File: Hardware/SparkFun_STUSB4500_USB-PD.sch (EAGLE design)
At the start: 47 parts, among them J4 QWIIC, Q1 7.6A/30V/29mΩ, U1 STUSB4500, U2 3.3V

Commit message: v01
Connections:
- net ALERT renamed !ALERT
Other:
- note added: "ADDR0 and ADDR1 sets I2C address: ADDR0 | ADDR1 | Address 0 | 0 | 0x28* 1 | 0 | 0x29 0 | 1 | 0x2A 1 | 1 | 0x2B * Default Address"
- note added: "VIN: 4.1 - 22V"
- note removed: "ADDR0 and ADDR1 sets I2C address: ADDR0 | ADDR1 | Address 0 | 0 | 0x28 1 | 0 | 0x29 0 | 1 | 0x2A 1 | 1 | 0x2B"
- note removed: "VCC: 4.1 - 22V"

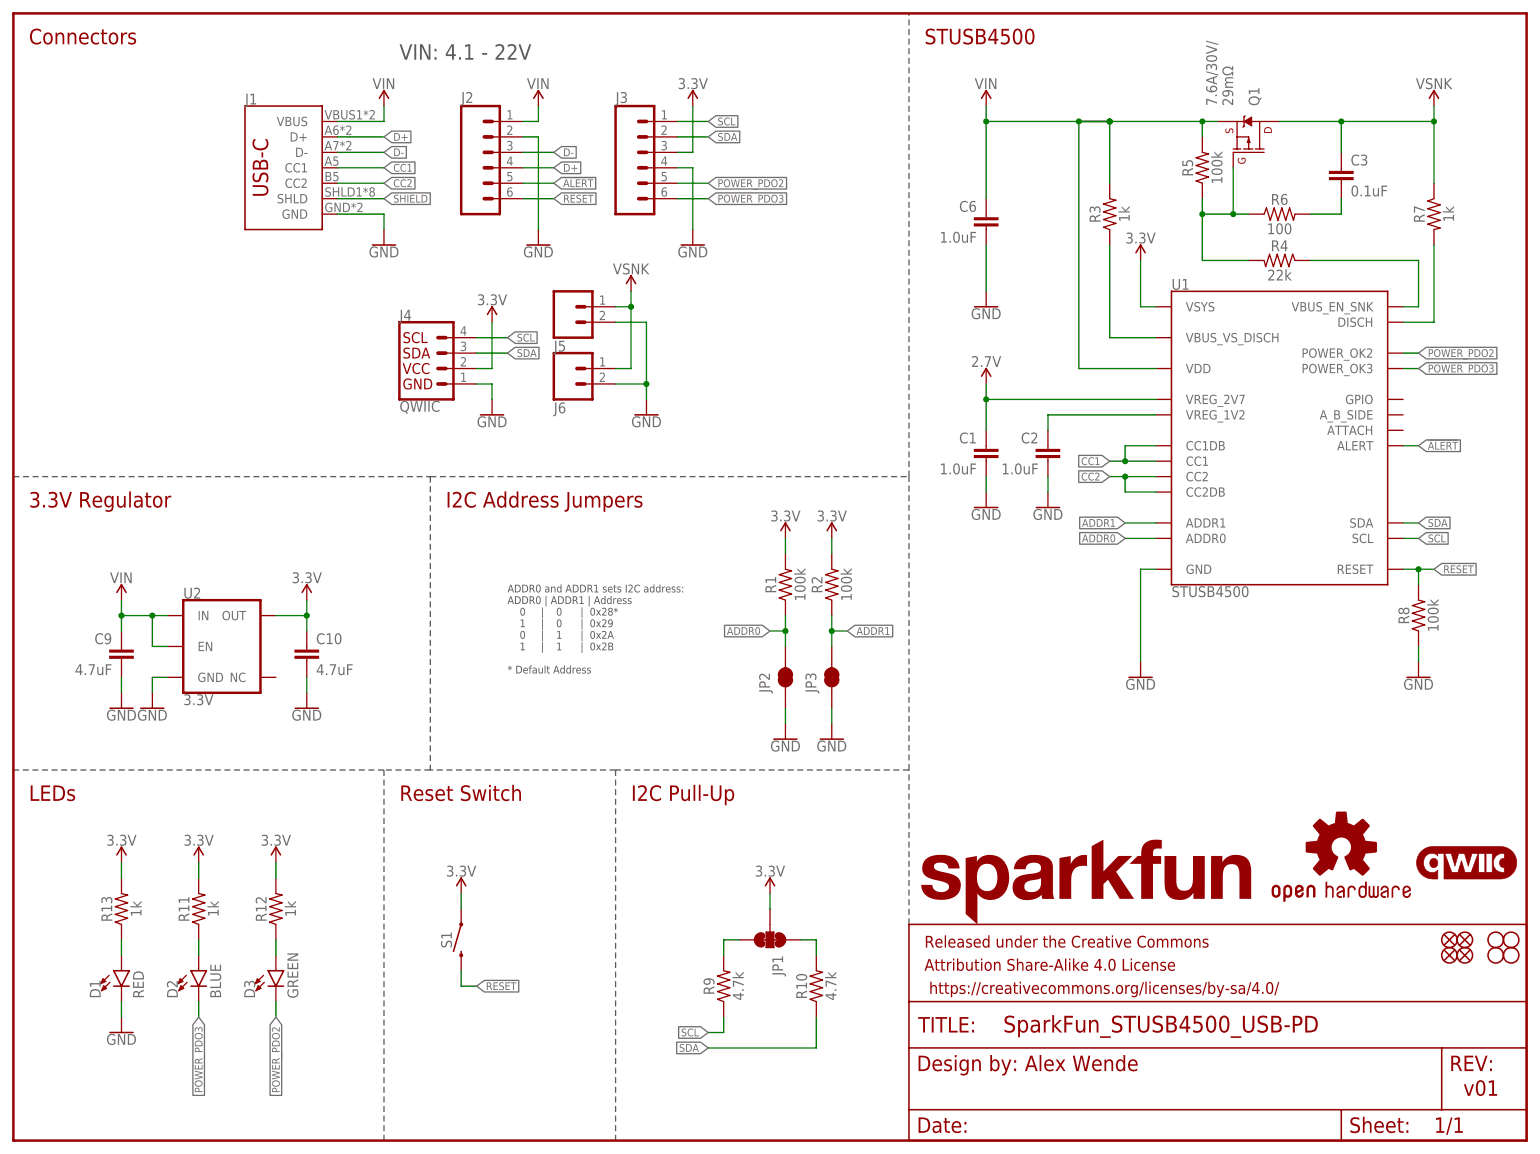
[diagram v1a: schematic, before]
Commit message: v02
-Added ESD protection diodes to VIN,VSNK, CC1, CC2
-Removed 3.3V LDO and replaced with the internal 2.7V regulated output of the STUSB4500.
-Added reverse current protection to the 2.7V regulator when VDD > 2.7V
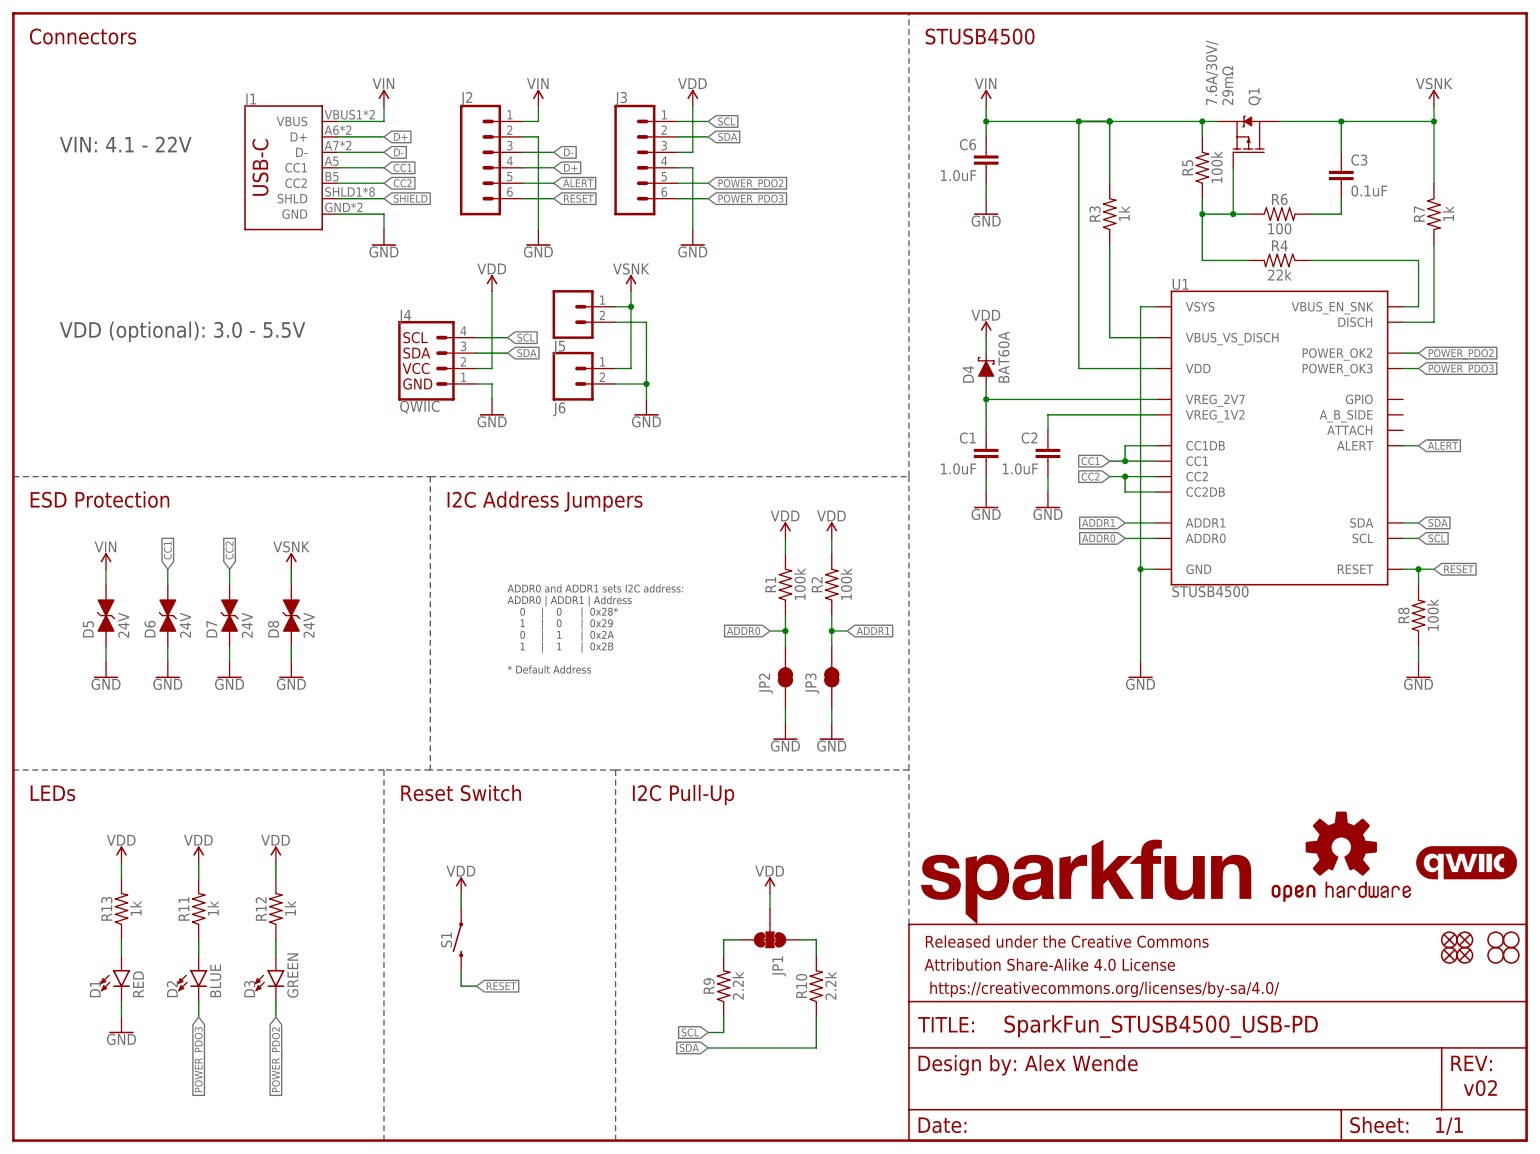
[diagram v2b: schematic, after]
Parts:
- removed C10, C9: 4.7uF, SparkFun-Capacitors:4.7UF-0603-35V-(20%)
- removed U2: 3.3V, SparkFun-IC-Power:AP7380-33W5-7
- added D4: BAT60A, SparkFun-DiscreteSemi:DIODE-SCHOTTKY-BAT60A
- added D5, D6, D7, D8: 24V, SparkFun-DiscreteSemi:DIODE_TVS
- LOGO3: value QWIIC_LOGO_5MM -> QWIIC_LOGO_3MM; device SparkFun-Aesthetics:QWIIC_LOGO_5MM -> SparkFun-Aesthetics:QWIIC_LOGO_3MM
- Q1: value 7.6A/30V/29mΩ -> 9A/30V/15mΩ; device SparkFun-DiscreteSemi:MOSFET_PCH-SI2369DS-T1-GE3 -> stusb4500:MOSFET_PCH-STL9P3LLH6
- R10, R9: value 4.7k -> 2.2k; device SparkFun-Resistors:4.7KOHM-0603-1/10W-1% -> SparkFun-Resistors:2.2KOHM-0603-1/10W-1%
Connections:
- removed net 3.3V: C10.1, J3.3, J4.2, JP1.2, R1.2, R11.2, R12.2, R13.2, R2.2, S1.1, U1.VSYS, U2.OUT
- new net VDD: D4.C, J3.3, J4.2, JP1.2, R1.2, R11.2, R12.2, R13.2, R2.2, S1.1
- net 2.7V: now also D4.A
- net CC1: now also D6.C
- net CC2: now also D7.C
- net GND: now also D5.A, D6.A, D7.A, D8.A, U1.VSYS; no longer C10.2, C9.2, U2.GND
- net VIN: now also D5.C; no longer C9.1, U2.EN, U2.IN
- net VSNK: now also D8.C
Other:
- note added: "ESD Protection"
- note added: "VDD (optional): 3.0 - 5.5V"
- note added: "v02"
- note removed: "3.3V Regulator"
- note removed: "v01"
- moved on the sheet: C6

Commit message: v20
- Updated Labels
- Connected VSYS to VDD
- Replaced Power LED with GPIO LED
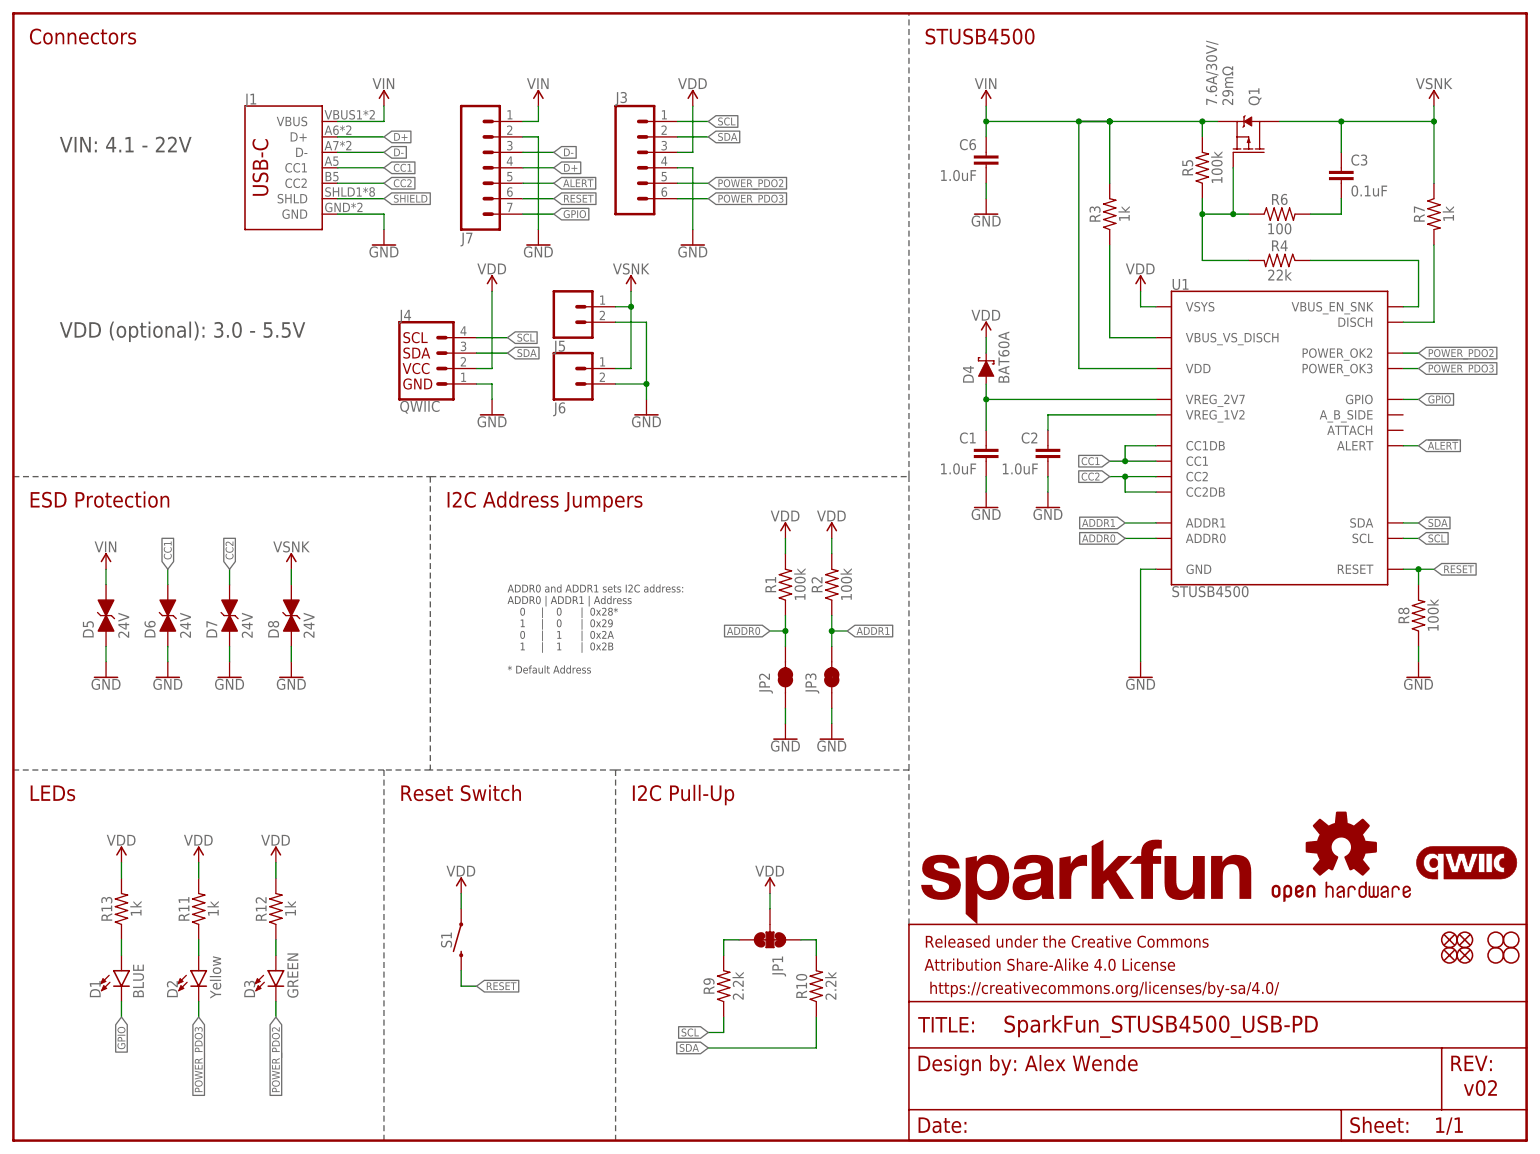
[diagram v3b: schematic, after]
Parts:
- removed J2: (no value), SparkFun-Connectors:CONN_06NO_SILK_NO_POP
- added J7: (no value), SparkFun-Connectors:CONN_07NO_SILK
- D1: value RED -> BLUE; device SparkFun-LED:LED-RED0603 -> SparkFun-LED:LED-BLUE0603
- D2: value BLUE -> Yellow; device SparkFun-LED:LED-BLUE0603 -> SparkFun-LED:LED-YELLOW0603
- LOGO3: value QWIIC_LOGO_3MM -> QWIIC_LOGO_5MM; device SparkFun-Aesthetics:QWIIC_LOGO_3MM -> SparkFun-Aesthetics:QWIIC_LOGO_5MM
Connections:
- new net GPIO: D1.C, J7.7, U1.GPIO
- net !ALERT: now also J7.5; no longer J2.5
- net D+: now also J7.4; no longer J2.4
- net D-: now also J7.3; no longer J2.3
- net GND: now also J7.2; no longer D1.C, J2.2, U1.VSYS
- net RESET: now also J7.6; no longer J2.6
- net VDD: now also U1.VSYS
- net VIN: now also J7.1; no longer J2.1
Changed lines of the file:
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@@
 <part name="SUPPLY10" library="SparkFun-PowerSymbols" deviceset="VOUT" device="" value="VSNK"/>
 <part name="S1" library="SparkFun-Switches" deviceset="MOMENTARY-SWITCH-SPST" device="-SMD-4.6X2.8MM" value=""/>
-<part name="D1" library="SparkFun-LED" deviceset="LED-RED" device="0603" value="RED"/>
+<part name="D1" library="SparkFun-LED" deviceset="LED-BLUE" device="0603" value="BLUE"/>
 <part name="R13" library="SparkFun-Resistors" deviceset="1KOHM" device="-0603-1/10W-1%" value="1k"/>
-<part name="GND16" library="SparkFun-PowerSymbols" deviceset="GND" device=""/>
-<part name="J2" library="SparkFun-Connectors" deviceset="CONN_06" device="NO_SILK_NO_POP"/>
 <part name="J3" library="SparkFun-Connectors" deviceset="CONN_06" device="NO_SILK_NO_POP"/>
-<part name="D2" library="SparkFun-LED" deviceset="LED-BLUE" device="0603" value="BLUE"/>
+<part name="D2" library="SparkFun-LED" deviceset="LED-YELLOW" device="0603" value="Yellow"/>
 <part name="D3" library="SparkFun-LED" deviceset="LED-GREEN" device="0603" value="GREEN"/>
 <part name="R11" library="SparkFun-Resistors" deviceset="1KOHM" device="-0603-1/10W-1%" value="1k"/>
@@
 <part name="LOGO1" library="SparkFun-Aesthetics" deviceset="OSHW-LOGO" device="S"/>
 <part name="LOGO2" library="SparkFun-Aesthetics" deviceset="SFE_LOGO_NAME" device=".1_INCH"/>
-<part name="LOGO3" library="SparkFun-Aesthetics" deviceset="QWIIC_LOGO" device="_3MM" value="QWIIC_LOGO_3MM"/>
+<part name="LOGO3" library="SparkFun-Aesthetics" deviceset="QWIIC_LOGO" device="_5MM" value="QWIIC_LOGO_5MM"/>
 <part name="GND10" library="SparkFun-PowerSymbols" deviceset="GND" device=""/>
 <part name="GND12" library="SparkFun-PowerSymbols" deviceset="GND" device=""/>
@@
 <part name="SUPPLY16" library="SparkFun-PowerSymbols" deviceset="VDD" device=""/>
 <part name="SUPPLY19" library="SparkFun-PowerSymbols" deviceset="VDD" device=""/>
+<part name="SUPPLY1" library="SparkFun-PowerSymbols" deviceset="VDD" device=""/>
+<part name="J7" library="SparkFun-Connectors" deviceset="CONN_07" device="NO_SILK"/>
 </parts>
 <sheets>
@@
 <attribute name="VALUE" x="19.304" y="38.1" size="1.778" layer="96" font="vector" rot="R90" align="top-center"/>
 </instance>
-<instance part="GND16" gate="1" x="17.78" y="17.78" smashed="yes">
-<attribute name="VALUE" x="17.78" y="17.526" size="1.778" layer="96" font="vector" align="top-center"/>
-</instance>
-<instance part="J2" gate="G$1" x="78.74" y="162.56" smashed="yes" rot="MR180">
-<attribute name="VALUE" x="73.66" y="172.466" size="1.778" layer="96" font="vector" rot="MR180"/>
-<attribute name="NAME" x="73.66" y="170.688" size="1.778" layer="95" font="vector"/>
-</instance>
 <instance part="J3" gate="G$1" x="104.14" y="162.56" smashed="yes" rot="MR180">
 <attribute name="VALUE" x="99.06" y="172.466" size="1.778" layer="96" font="vector" rot="MR180"/>
@@
 <attribute name="VALUE" x="134.62" y="101.854" size="1.778" layer="96" align="bottom-center"/>
 </instance>
+<instance part="SUPPLY1" gate="VDD" x="185.42" y="139.7" smashed="yes">
+<attribute name="VALUE" x="185.42" y="142.494" size="1.778" layer="96" align="bottom-center"/>
+</instance>
+<instance part="J7" gate="J1" x="78.74" y="162.56" smashed="yes" rot="MR180">
+<attribute name="VALUE" x="73.66" y="172.466" size="1.778" layer="96" font="vector" rot="MR180"/>
+<attribute name="NAME" x="73.66" y="149.352" size="1.778" layer="95" font="vector" rot="MR180"/>
+</instance>
 </instances>
 <busses>
@@
 </segment>
 <segment>
-<pinref part="D1" gate="G$1" pin="C"/>
-<pinref part="GND16" gate="1" pin="GND"/>
-<wire x1="17.78" y1="22.86" x2="17.78" y2="20.32" width="0.1524" layer="91"/>
-</segment>
-<segment>
 <pinref part="U1" gate="G$1" pin="GND"/>
 <pinref part="GND2" gate="1" pin="GND"/>
 <wire x1="187.96" y1="93.98" x2="185.42" y2="93.98" width="0.1524" layer="91"/>
 <wire x1="185.42" y1="93.98" x2="185.42" y2="78.74" width="0.1524" layer="91"/>
-<pinref part="U1" gate="G$1" pin="VSYS"/>
-<wire x1="187.96" y1="137.16" x2="185.42" y2="137.16" width="0.1524" layer="91"/>
-<wire x1="185.42" y1="137.16" x2="185.42" y2="93.98" width="0.1524" layer="91"/>
-<junction x="185.42" y="93.98"/>
-</segment>
-<segment>
-<pinref part="J2" gate="G$1" pin="2"/>
+</segment>
+<segment>
 <wire x1="83.82" y1="165.1" x2="86.36" y2="165.1" width="0.1524" layer="91"/>
 <pinref part="GND10" gate="1" pin="GND"/>
 <wire x1="86.36" y1="165.1" x2="86.36" y2="149.86" width="0.1524" layer="91"/>
+<pinref part="J7" gate="J1" pin="2"/>
 </segment>
 <segment>
@@
 </segment>
 <segment>
-<pinref part="J2" gate="G$1" pin="4"/>
 <wire x1="83.82" y1="160.02" x2="88.9" y2="160.02" width="0.1524" layer="91"/>
 <label x="88.9" y="160.02" size="1.27" layer="95" font="vector" rot="MR180" xref="yes"/>
+<pinref part="J7" gate="J1" pin="4"/>
 </segment>
 </net>
@@
 </segment>
 <segment>
-<pinref part="J2" gate="G$1" pin="3"/>
 <wire x1="83.82" y1="162.56" x2="88.9" y2="162.56" width="0.1524" layer="91"/>
 <label x="88.9" y="162.56" size="1.27" layer="95" font="vector" rot="MR180" xref="yes"/>
+<pinref part="J7" gate="J1" pin="3"/>
 </segment>
 </net>
@@
 </segment>
 <segment>
-<pinref part="J2" gate="G$1" pin="5"/>
 <wire x1="83.82" y1="157.48" x2="88.9" y2="157.48" width="0.1524" layer="91"/>
 <label x="88.9" y="157.48" size="1.27" layer="95" font="vector" rot="MR180" xref="yes"/>
+<pinref part="J7" gate="J1" pin="5"/>
 </segment>
 </net>
@@
 </segment>
 <segment>
-<pinref part="J2" gate="G$1" pin="6"/>
 <wire x1="83.82" y1="154.94" x2="88.9" y2="154.94" width="0.1524" layer="91"/>
 <label x="88.9" y="154.94" size="1.27" layer="95" font="vector" rot="MR180" xref="yes"/>
+<pinref part="J7" gate="J1" pin="6"/>
 </segment>
 </net>
@@
 </segment>
 <segment>
-<pinref part="J2" gate="G$1" pin="1"/>
 <wire x1="83.82" y1="167.64" x2="86.36" y2="167.64" width="0.1524" layer="91"/>
 <wire x1="86.36" y1="170.18" x2="86.36" y2="167.64" width="0.1524" layer="91"/>
 <pinref part="SUPPLY18" gate="G$1" pin="VIN"/>
+<pinref part="J7" gate="J1" pin="1"/>
 </segment>
 <segment>
@@
 <pinref part="SUPPLY5" gate="VDD" pin="VDD"/>
 </segment>
-</net>
+<segment>
+<pinref part="U1" gate="G$1" pin="VSYS"/>
+<wire x1="187.96" y1="137.16" x2="185.42" y2="137.16" width="0.1524" layer="91"/>
+<wire x1="185.42" y1="137.16" x2="185.42" y2="139.7" width="0.1524" layer="91"/>
+<pinref part="SUPPLY1" gate="VDD" pin="VDD"/>
+</segment>
+</net>
+<net name="GPIO" class="0">
+<segment>
+<pinref part="U1" gate="G$1" pin="GPIO"/>
+<wire x1="228.6" y1="121.92" x2="231.14" y2="121.92" width="0.1524" layer="91"/>
+<label x="231.14" y="121.92" size="1.27" layer="95" xref="yes"/>
+</segment>
+<segment>
+<pinref part="D1" gate="G$1" pin="C"/>
+<wire x1="17.78" y1="22.86" x2="17.78" y2="20.32" width="0.1524" layer="91"/>
+<label x="17.78" y="20.32" size="1.27" layer="95" rot="R270" xref="yes"/>
+</segment>
+<segment>
+<pinref part="J7" gate="J1" pin="7"/>
+<wire x1="83.82" y1="152.4" x2="88.9" y2="152.4" width="0.1524" layer="91"/>
+<label x="88.9" y="152.4" size="1.27" layer="95" xref="yes"/>
+</segment>
+</net>
